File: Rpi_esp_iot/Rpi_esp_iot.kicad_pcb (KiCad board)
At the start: 2 copper layers, 120 x 70 mm, 171 parts, among them J1 Conn_01x03, J2 Conn_01x03, J3 USB_C_Receptacle_USB2.0_16P, J6 SIM8066-6-1-14-01-A_REVA, Q1 MMDT3904, Q2 NMOS, Q3 CSD18540Q5B, Q4 CSD18540Q5B, Q5 NMOS, Q6 MMDT3904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

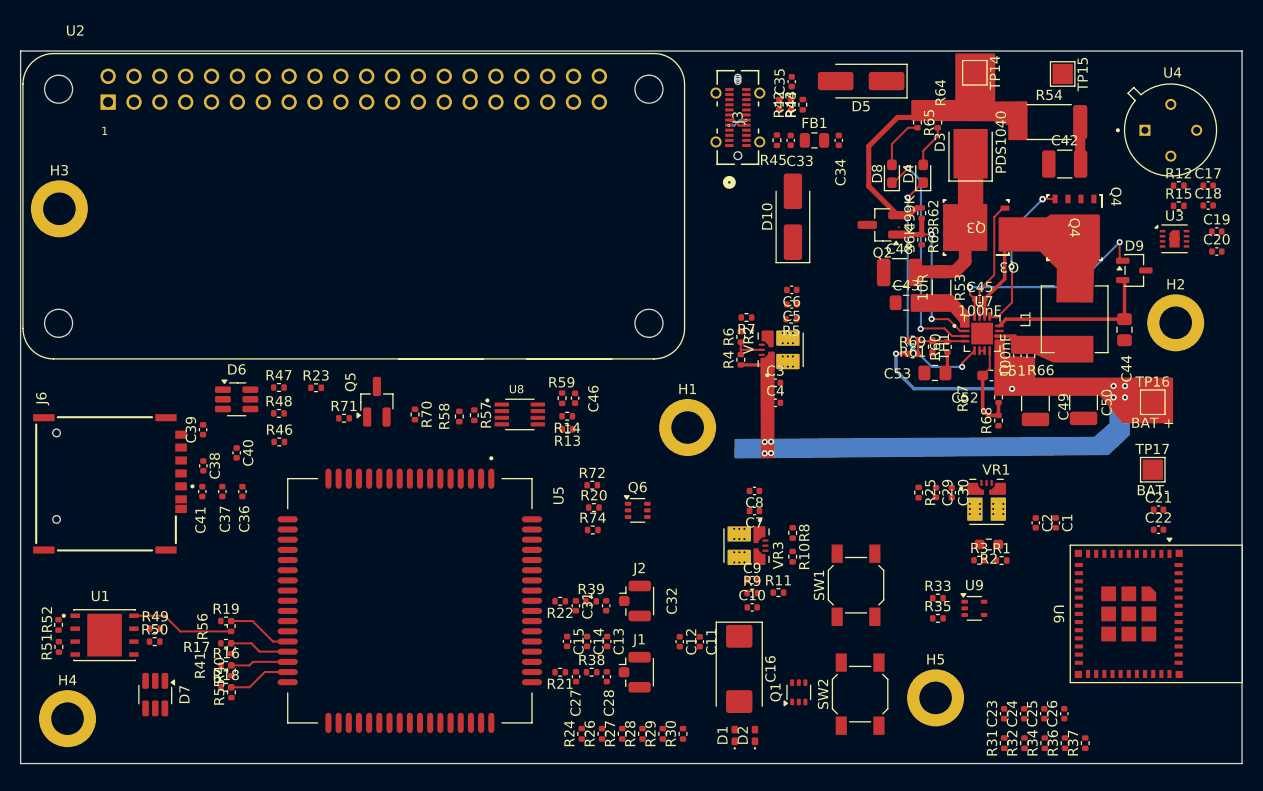
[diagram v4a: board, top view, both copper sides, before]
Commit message: Routing Complete
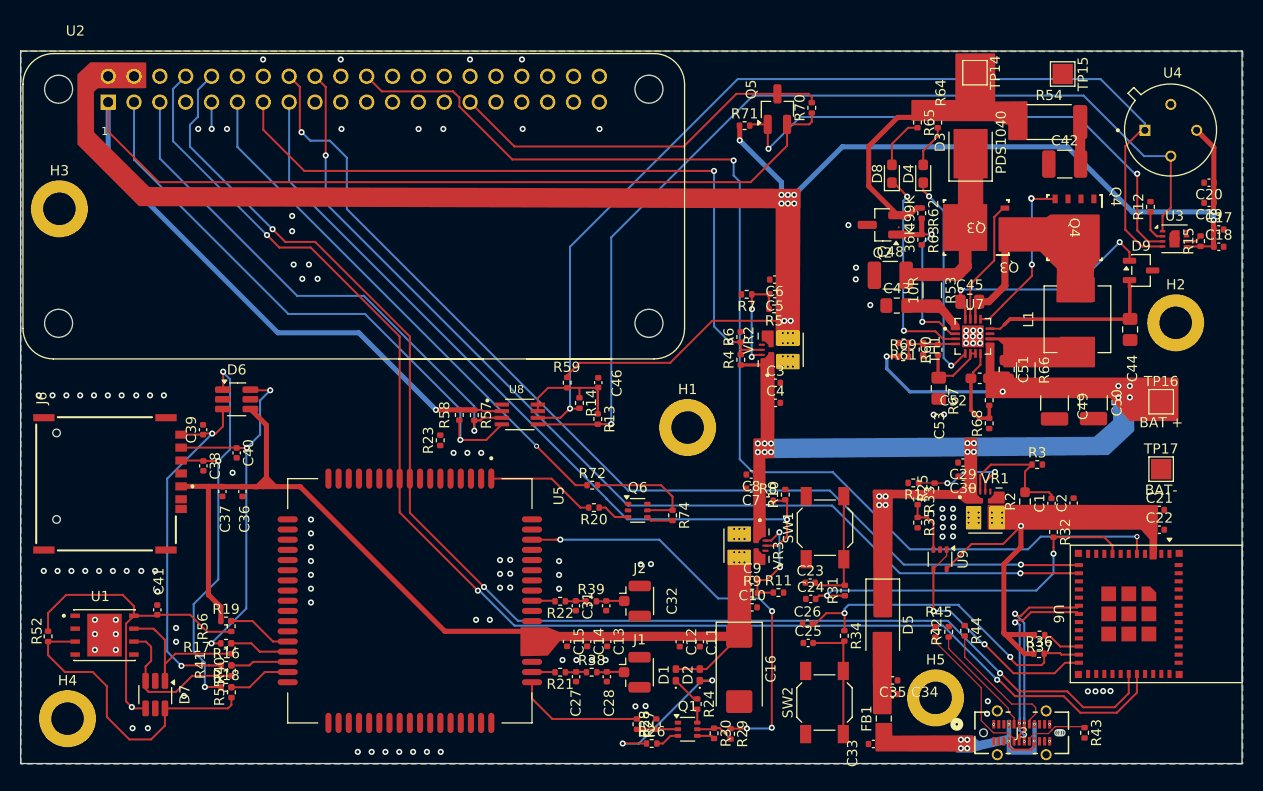
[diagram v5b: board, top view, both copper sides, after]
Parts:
- removed D10: SS26, Diode_SMD:D_SMA_Handsoldering
- removed R46, R47, R48, R49, R50, R51: 0R, Resistor_SMD:R_0402_1005Metric
- C45, C51: footprint Capacitor_SMD:C_0402_1005Metric -> Resistor_SMD:R_0805_2012Metric
- R66: footprint Resistor_SMD:R_0402_1005Metric -> Resistor_SMD:R_1206_3216Metric_Pad1.30x1.75mm_HandSolder
- moved R43 67.6 mm to (194.9, 116.2), turned to -90 degrees
- moved J3 66.6 mm to (188.8, 116.2), turned to 0 degrees
- moved C33 59.9 mm to (174.2, 117.2), turned to 0 degrees
- moved C35 59.6 mm to (176.1, 111.0), turned to 180 degrees
- moved FB1 57.2 mm to (175.2, 114.8), turned to 90 degrees
- moved R44 54.8 mm to (183.2, 106.1)
- moved C34 54.7 mm to (176.1, 112.3), turned to 180 degrees
- moved R42 54.1 mm to (181.6, 106.2)
- moved D5 53.5 mm to (175.1, 105.5), turned to -90 degrees
- moved R45 50.8 mm to (180.2, 106.2), turned to -90 degrees
- moved R70 49.3 mm to (168.1, 54.8), turned to 90 degrees
- moved R71 48.7 mm to (161.5, 56.5)
- moved Q5 48.7 mm to (164.8, 54.9)
- moved C26 26.7 mm to (167.7, 105.4), turned to 0 degrees
- moved C25 24.2 mm to (167.8, 107.3), turned to 0 degrees
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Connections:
- net ESP_GPIO12_USB_D- renamed ESP_USB_D_N
- net ESP_GPIO13_USB_D+ renamed ESP_USB_D_P
- C29 pad 1: +V_SUPPLY -> +Vbat
- C30 pad 1: +V_SUPPLY -> +Vbat
- C38 pad 1: /RST_EN -> SIM_RST
- C39 pad 1: /CLK_EN -> SIM_CLK
- C40 pad 1: /DATA_EN -> SIM_DATA
- D5 pad 1: +V_SUPPLY -> +Vbat
- D6 pad 1: /RST_EN -> SIM_RST
- D6 pad 3: /CLK_EN -> SIM_CLK
- D6 pad 6: /DATA_EN -> SIM_DATA
- D7 pad 1: /ES_RST_EN -> ESIM_RST
- D7 pad 3: /ES_CLK_EN -> ESIM_CLK
- D7 pad 6: /ES_DATA_EN -> ESIM_DATA
- J6 pad C2: /RST_EN -> SIM_RST
- J6 pad C3: /CLK_EN -> SIM_CLK
- J6 pad C7: /DATA_EN -> SIM_DATA
- R1 pad 1: GND -> Net-(VR1-EN)
- R19 pad 1: PSIM_VCC -> SIM_VCC
- R25 pad 1: +V_SUPPLY -> +Vbat
- R25 pad 2: GND -> Net-(VR1-EN)
- R37 pad 2: +3.3V -> +3.3V_ESP
- R52 pad 2: /ES_DATA_EN -> ESIM_DATA
- U1 pad 3: /ES_DATA_EN -> ESIM_DATA
- U1 pad 6: /ES_CLK_EN -> ESIM_CLK
- U1 pad 7: /ES_RST_EN -> ESIM_RST
- U9 pad 5: +3V3 -> +3.3V_ESP
- VR1 pad 1: +V_SUPPLY -> +Vbat
- VR1 pad 6: GND -> Net-(VR1-EN)
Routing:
- net ESP_TX: track 0.00 -> 137.7 mm, vias 0 -> 3
- net ESP_RX: track 0.00 -> 135.4 mm, vias 0 -> 3
- net +3V3_RPI: track 0.00 -> 134.8 mm, vias 0 -> 1
- net ESP_GPIO2: track 0.00 -> 114.5 mm, vias 0 -> 2
- net ESP_GPIO0: track 0.00 -> 102.9 mm, vias 0 -> 2
- net ESP_GPIO1: track 0.00 -> 102.0 mm, vias 0 -> 2
- net SNS_I2C_SCL: track 0.00 -> 101.4 mm, vias 0 -> 1
- net SNS_I2C_SDA: track 0.00 -> 96.5 mm, vias 0 -> 1
- net +5V_RPi: track 0.00 -> 93.2 mm, vias 0 -> 11
- net SIM_PWR_EN: track 0.00 -> 79.7 mm, vias 0 -> 1
- net SIM_VCC: track 0.00 -> 72.9 mm
- net RPI_PWR_EN: track 3.31 -> 70.5 mm, vias 0 -> 2
- net RPI_SDA: track 0.00 -> 57.4 mm, vias 0 -> 1
- net RPI_SCL: track 0.00 -> 52.7 mm, vias 0 -> 1
- net SHT_ALT: track 0.00 -> 52.6 mm, vias 0 -> 2
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- added copper zone on B.Cu, net GND
- added copper zone on F.Cu, net GND
